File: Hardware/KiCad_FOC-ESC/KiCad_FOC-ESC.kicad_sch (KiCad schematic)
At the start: 0 parts

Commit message: added components (#6)
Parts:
- added U1: STM32G473RCTx, Package_QFP:LQFP-64_10x10mm_P0.5mm, symbol MCU_ST_STM32G4:STM32G473RCTx
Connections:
- new net: U1.15 (VSS), U1.31 (VSS), U1.47 (VSS), U1.63 (VSS)
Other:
- added sheet FET_Driver (FET_Driver.kicad_sch)
- added sheet FETs (FETs.kicad_sch)
- added sheet Vref_1V65 (Vref_1V65.kicad_sch)
- added sheet angle_sens (angle_sens.kicad_sch)
- added sheet current_sens (current_sens.kicad_sch)

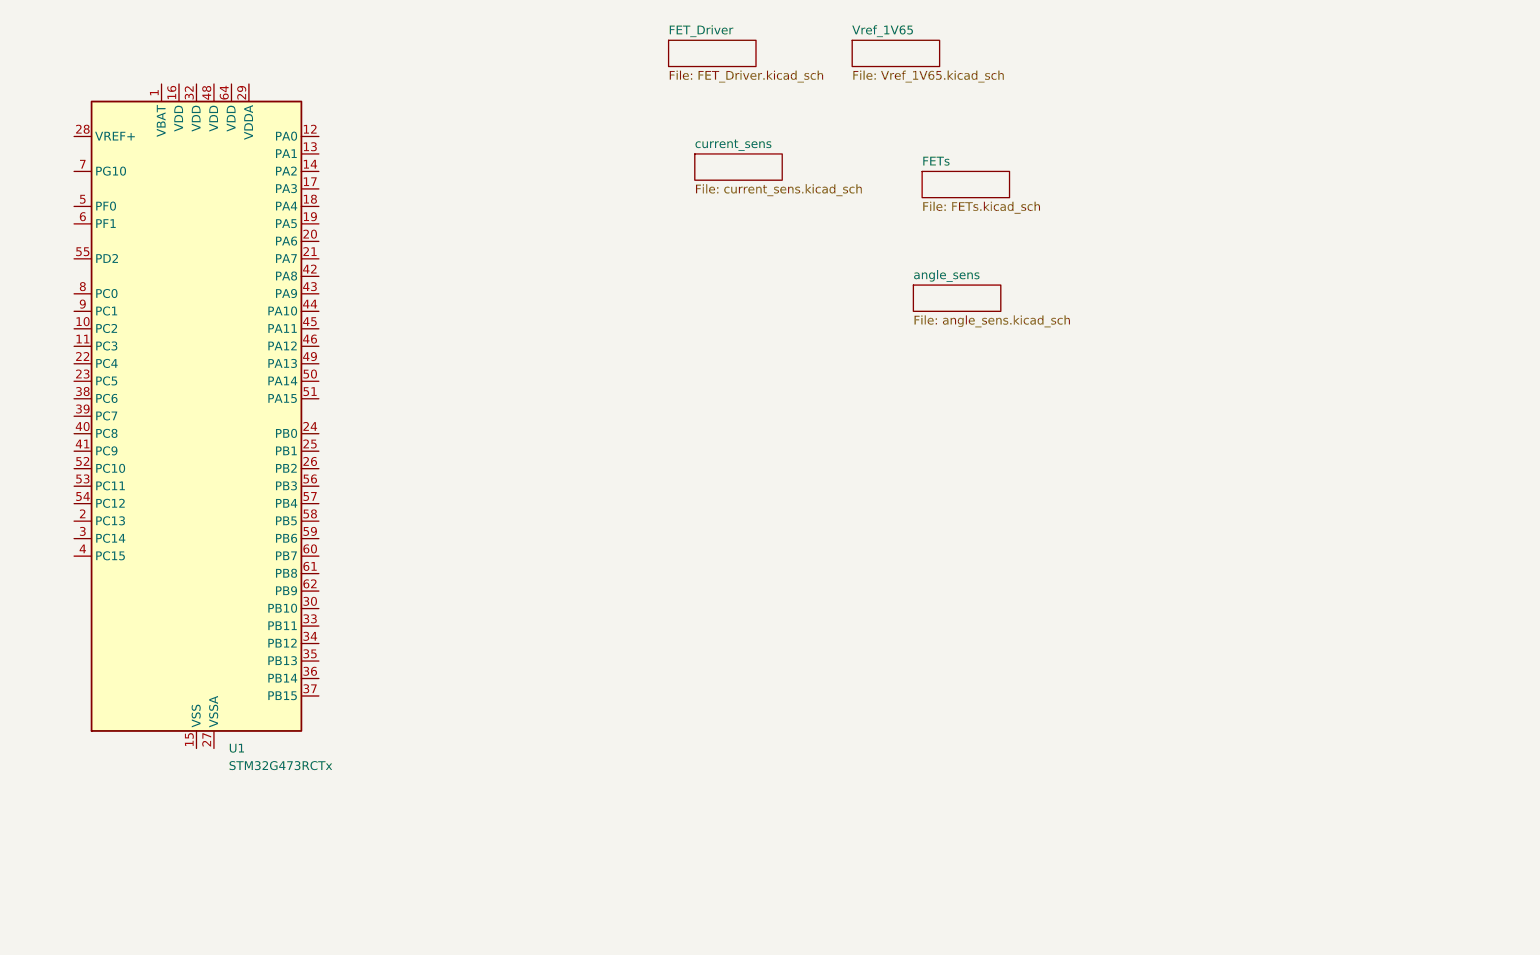
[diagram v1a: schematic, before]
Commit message: inited Software (#7)
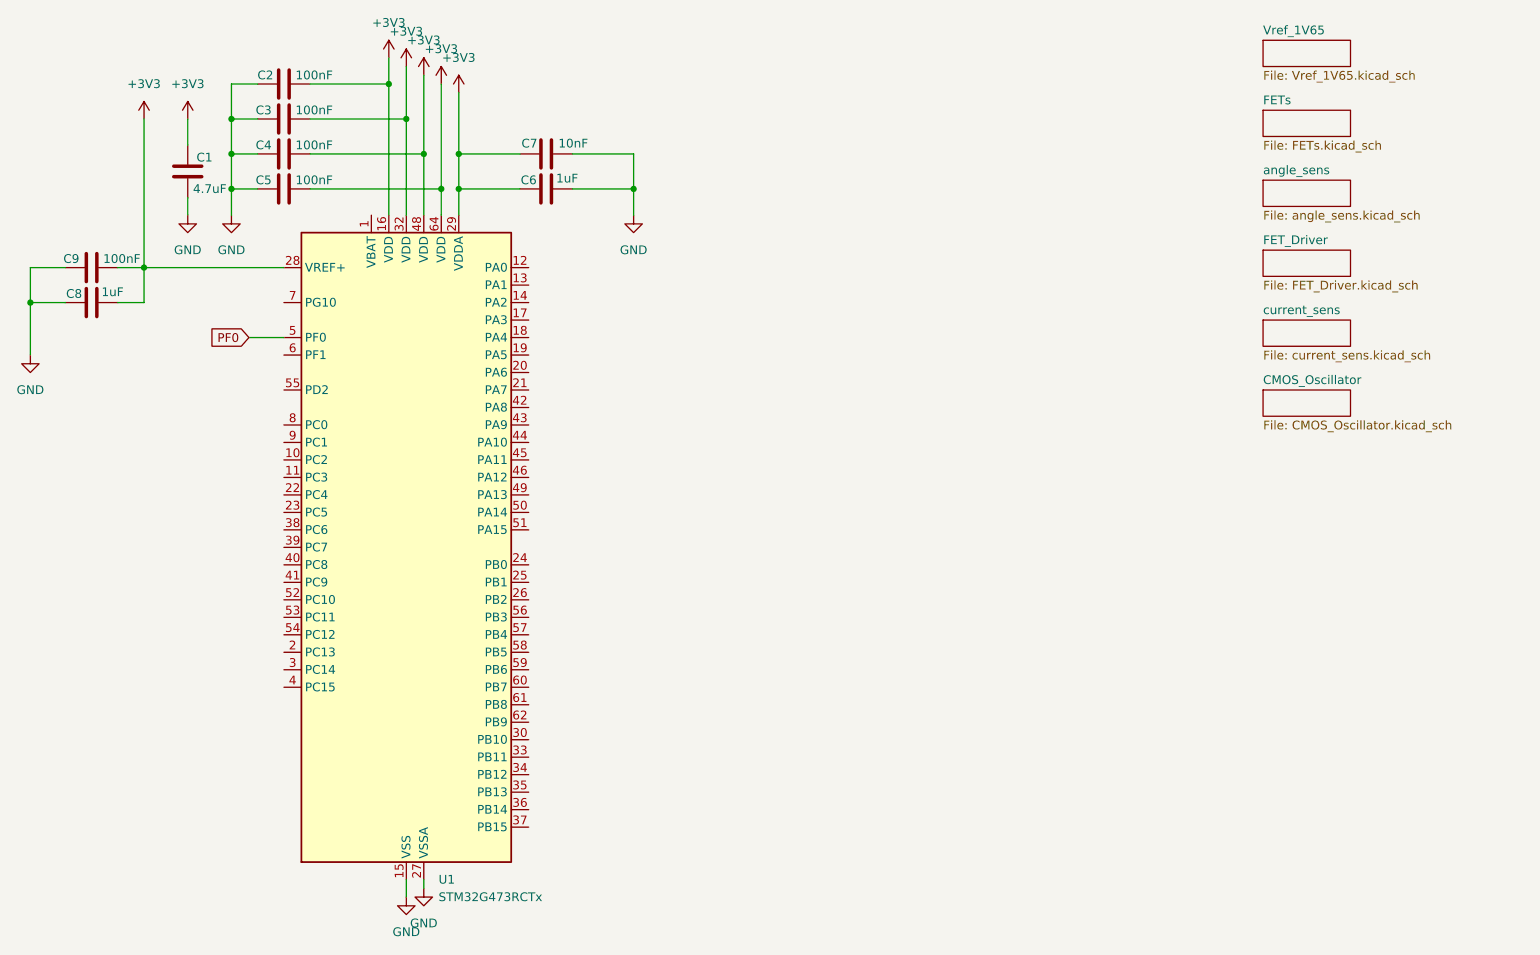
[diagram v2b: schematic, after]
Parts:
- added C1: 4.7uF, Capacitor_SMD:C_0603_1608Metric, symbol Device:C
- added C2, C3, C4, C5, C9: 100nF, Capacitor_SMD:C_0402_1005Metric, symbol Device:C
- added C6, C8: 1uF, Capacitor_SMD:C_0603_1608Metric, symbol Device:C
- added C7: 10nF, Capacitor_SMD:C_0402_1005Metric, symbol Device:C
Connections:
- net GND: now reaches U1.15 (VSS), U1.31 (VSS), U1.47 (VSS), U1.63 (VSS)
- net GND: now also U1.27 (VSSA), C1.2, C2.1, C3.1, C4.1, C5.1, C6.2, C7.2, C8.1, C9.1
- net +3V3: now reaches U1.16 (VDD)
- net +3V3: now also U1.28 (VREF+), U1.29 (VDDA), U1.32 (VDD), U1.48 (VDD), U1.64 (VDD), C1.1, C2.2, C3.2, C4.2, C5.2, C6.1, C7.1, C8.2, C9.2
- net PF0: now reaches U1.5 (PF0)
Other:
- added sheet CMOS_Oscillator (CMOS_Oscillator.kicad_sch)
- moved on the sheet: U1

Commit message: ready
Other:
- added sheet Debbug (Debbug.kicad_sch)
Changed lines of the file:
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@@
+	)
+	(sheet
+		(at 209.55 90.17)
+		(size 12.7 3.81)
+		(exclude_from_sim no)
+		(in_bom yes)
+		(on_board yes)
+		(dnp no)
+		(fields_autoplaced yes)
+		(stroke
+			(width 0.1524)
+			(type solid)
+		)
+		(fill
+			(color 0 0 0 0)
+		)
+		(property "Sheetname" "Debbug"
+			(at 209.55 89.4584 0)
+			(show_name no)
+			(do_not_autoplace no)
+			(effects
+				(font
+					(size 1.27 1.27)
+				)
+				(justify left bottom)
+			)
+		)
+		(property "Sheetfile" "Debbug.kicad_sch"
+			(at 209.55 94.5646 0)
+			(show_name no)
+			(do_not_autoplace no)
+			(effects
+				(font
+					(size 1.27 1.27)
+				)
+				(justify left top)
+			)
+		)
+		(instances
+			(project "KiCad_FOC-ESC"
+				(path "/5aa129d7-7a76-48d9-8008-691cf751c140"
+					(page "8")
+				)
+			)
+		)
 	)
 	(sheet
